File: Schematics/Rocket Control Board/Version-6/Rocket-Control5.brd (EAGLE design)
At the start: 20.3 x 38.1 mm, 28 parts

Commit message: Tons of Changes
Too many to describe. Most of the semester board design and rocket club
stuff.
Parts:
- removed CRYSTAL-CAP-1, CRYSTAL-CAP-2: 6.8pF, RocketControlBoard:C0603
- removed OSC-CRYSTAL: ABS25-32.768KHZ-6-T, RocketControlBoard:4-SOJ:CRYSTAL
- added OSC-CAPACITOR-1, OSC-CAPACITOR-2: 22pF, RocketControlBoard:C0603
- added U$1: ABS07-32.768KHZ-T, RocketControlBoard:ABS07-32.768KHZ-T
- moved FERRITE-BEAD 1.91 mm to (16.4, 8.81)
- moved ANALOG-CAPACITOR-1 1.40 mm to (15.4, 11.6)
- moved ANALOG-CAPACITOR-2 1.35 mm to (16.7, 11.6)
- moved AREF-CAPACITOR-2 0.98 mm to (14.2, 9.99)
- moved AREF-CAPACITOR-1 0.90 mm to (13.0, 9.31)
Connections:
- net CRYSTAL-A: now also OSC-CAPACITOR-1.2, U$1.P$2; no longer CRYSTAL-CAP-2.2, OSC-CRYSTAL.2:CRYSTAL
- net CRYSTAL-B: now also OSC-CAPACITOR-2.2, U$1.P$1; no longer CRYSTAL-CAP-1.2, OSC-CRYSTAL.1:CRYSTAL
- net GND: now also OSC-CAPACITOR-1.1, OSC-CAPACITOR-2.1; no longer CRYSTAL-CAP-1.1, CRYSTAL-CAP-2.1
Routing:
- net CRYSTAL-A: track 11.8 -> 5.55 mm
- net A1: track 9.97 -> 15.9 mm, vias 0 -> 1
- net CRYSTAL-B: track 10.8 -> 5.79 mm
- net GND: track 38.8 -> 36.2 mm, vias 5 -> 6
- net ANALOG-VDD: track 8.94 -> 7.34 mm
- net A2: track 7.52 -> 8.37 mm
- net A3: track 5.59 -> 6.17 mm

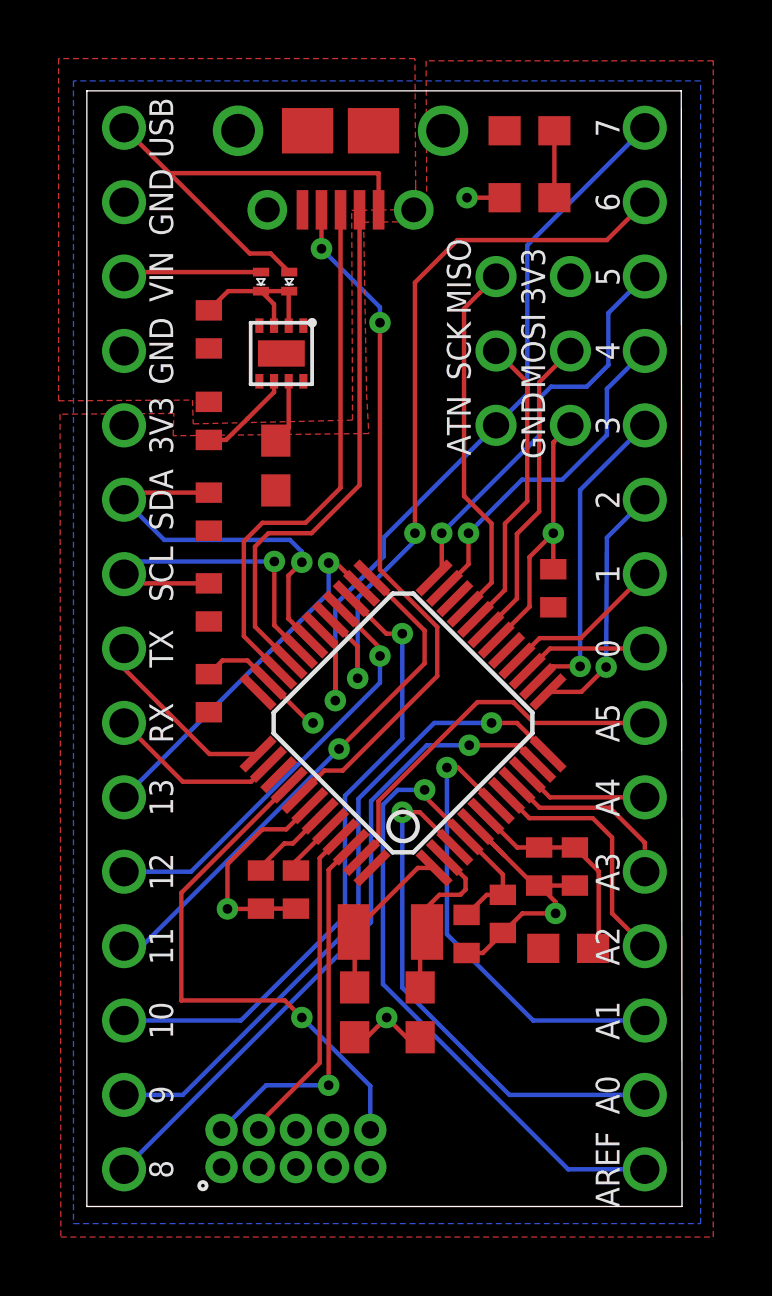
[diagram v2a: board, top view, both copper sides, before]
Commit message: New Crystal and Regualtor
Title
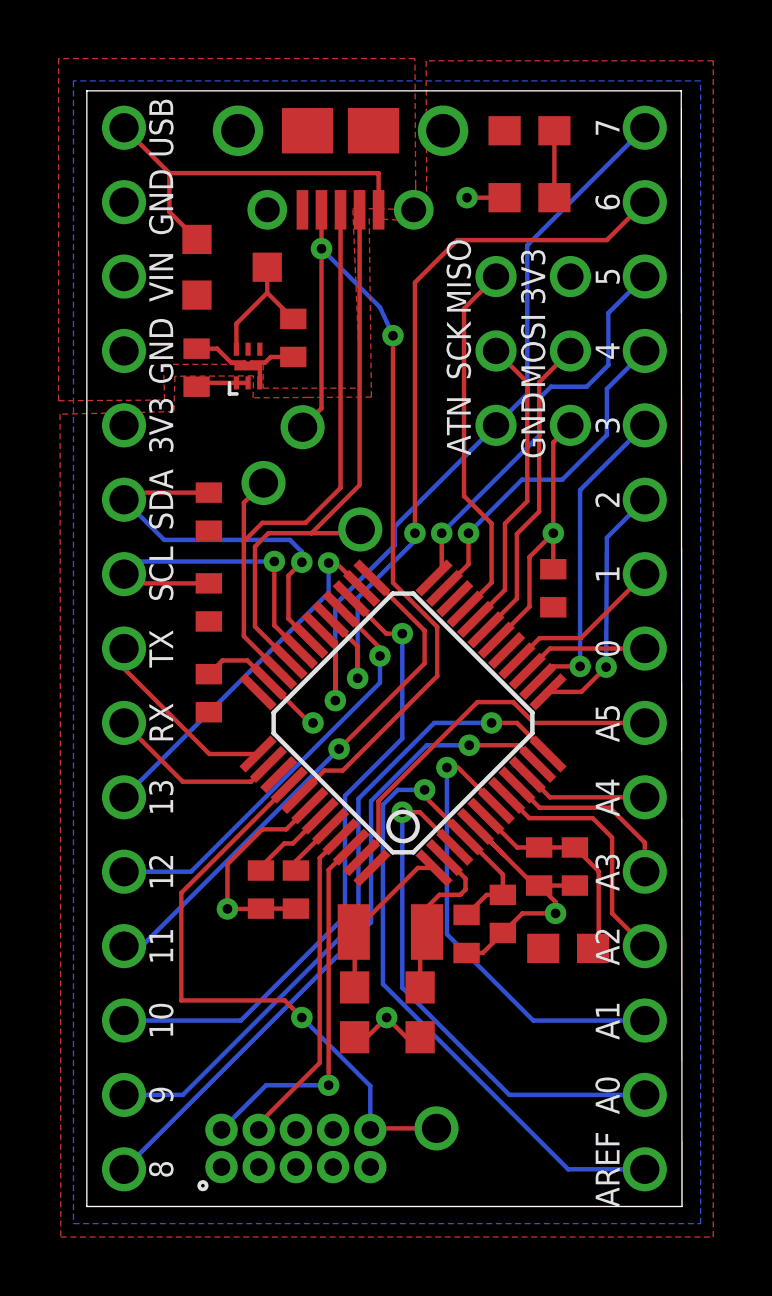
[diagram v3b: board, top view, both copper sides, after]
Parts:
- removed DIODE-USB, DIODE-VIN: CTS05S40,L3F, RocketControlBoard:SOD-882
- removed REGULATOR-3.3V: TPS62172DSGR, RocketControlBoard:8-WFDFN-EXPOSED-PAD
- removed REGULATOR-IN-CAPACITOR: 10uF, RocketControlBoard:C0402
- removed REGULATOR-OUT-CAPACITOR: 22uF, RocketControlBoard:C0402
- removed REGULATOR-OUT-INDUCTOR: 2.2uH, RocketControlBoard:C0603
- added REGULATOR-IN-CAPACITOR1: 10uF, RocketControlBoard:C0402
- added REGULATOR-OUT-CAPACITOR1: 22uF, RocketControlBoard:C0402
- added U$2: MIC5528, RocketControlBoard:MIC5528
- added U$3: DIODE-STANDARD, RocketControlBoard:DIODE-STANDARD
- added U$4, U$5, U$6, U$7: HEADER-HOLE, RocketControlBoard:HEADER-HOLE
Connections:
- removed net N$1: REGULATOR-3.3V.SW, REGULATOR-OUT-INDUCTOR.1
- net +3V3: now also REGULATOR-OUT-CAPACITOR1.1, U$2.VOUT@1, U$2.VOUT@2; no longer REGULATOR-3.3V.VOS, REGULATOR-OUT-CAPACITOR.2, REGULATOR-OUT-INDUCTOR.2
- net GND: now also REGULATOR-IN-CAPACITOR1.1, REGULATOR-OUT-CAPACITOR1.2, U$2.GND@1, U$2.GND@2; no longer REGULATOR-3.3V.AGND, REGULATOR-3.3V.EXPOSED-THERMAL-PAD, REGULATOR-3.3V.FB, REGULATOR-3.3V.PGND, REGULATOR-IN-CAPACITOR.1, REGULATOR-OUT-CAPACITOR.1
- net REG-VIN: now also REGULATOR-IN-CAPACITOR1.2, U$2.VIN, U$3.CATHODE; no longer DIODE-USB.P$2, DIODE-VIN.P$2, REGULATOR-3.3V.EN, REGULATOR-3.3V.VIN, REGULATOR-IN-CAPACITOR.2
- net SWD-06(RESET): now also U$5.P$1
- net USB: now also U$3.ANODE; no longer DIODE-USB.P$1
- net USB-ID: now also U$4.P$1
- net USB-N: now also U$6.P$1
- net USB-P: now also U$7.P$1
- net VIN: no longer DIODE-VIN.P$1
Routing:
- net USB-ID: track 23.9 -> 30.2 mm
- net VIN: track 4.74 -> 0.00 mm
- net GND: track 36.2 -> 40.9 mm
- net USB: track 16.1 -> 13.2 mm
- net SWD-06(RESET): track 18.0 -> 20.3 mm
- net USB-P: track 18.5 -> 20.7 mm
- net N$1: track 2.21 -> 0.00 mm
- net USB-N: track 18.2 -> 19.9 mm
- net +3V3: track 5.26 -> 3.88 mm
- net REG-VIN: track 5.59 -> 4.49 mm
